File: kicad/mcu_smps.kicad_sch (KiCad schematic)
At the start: 3 parts

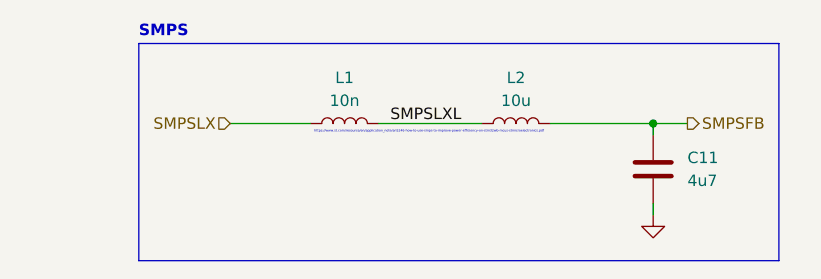
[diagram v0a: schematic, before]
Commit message: refactor(schematic): polish the schematic as much as possible - add new Basmala - fix netlist names almost EVERYWHERE, this is to help with net classes, and to help with building a good habit of naming nets properly - add a 100n capacitor to the SWD connector power pin - update many many other things EVERYWHERE
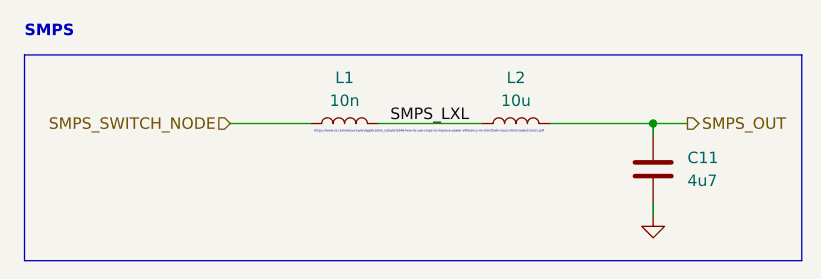
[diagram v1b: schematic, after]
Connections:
- net SMPSFB renamed SMPS_OUT
- net SMPSLX renamed SMPS_SWITCH_NODE
- net SMPSLXL renamed SMPS_LXL
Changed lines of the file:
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@@
 	)
 	(rectangle
-		(start 101.6 85.09)
-		(end 172.72 109.22)
+		(start 88.9 86.36)
+		(end 175.26 109.22)
 		(stroke
 			(width 0)
@@
 	(text "SMPS"
 		(exclude_from_sim no)
-		(at 101.6 83.82 0)
+		(at 88.9 83.82 0)
 		(effects
 			(font
@@
 		)
 	)
-	(label "SMPSLXL"
+	(label "SMPS_LXL"
 		(at 129.54 93.98 0)
 		(effects
@@
 		)
 	)
-	(hierarchical_label "SMPSFB"
+	(hierarchical_label "SMPS_OUT"
 		(shape output)
 		(at 162.56 93.98 0)
@@
 		)
 	)
-	(hierarchical_label "SMPSLX"
+	(hierarchical_label "SMPS_SWITCH_NODE"
 		(shape input)
 		(at 111.76 93.98 180)
